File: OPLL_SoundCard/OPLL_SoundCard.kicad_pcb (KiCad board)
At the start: 2 copper layers, 101.6 x 53.3 mm, 13 parts, among them P1 Digital, P10 CONN_01X01, P11 CONN_01X01, P12 CONN_01X01, P13 CONN_01X01, P2 Power, P3 Analog, P4 Analog, P5 PWM, P6 PWM, P7 Communication, P8 CONN_01X01, P9 CONN_01X01

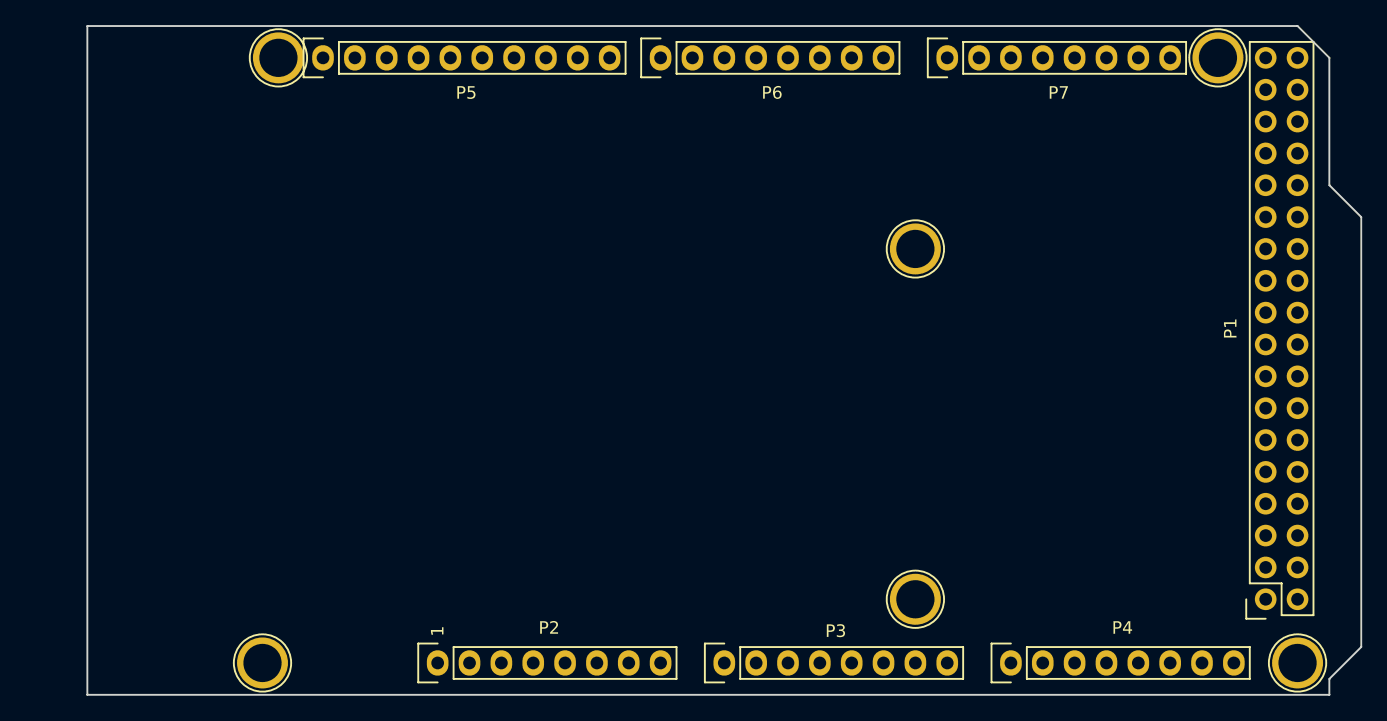
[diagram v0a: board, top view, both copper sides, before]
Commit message: PCB Soundcard
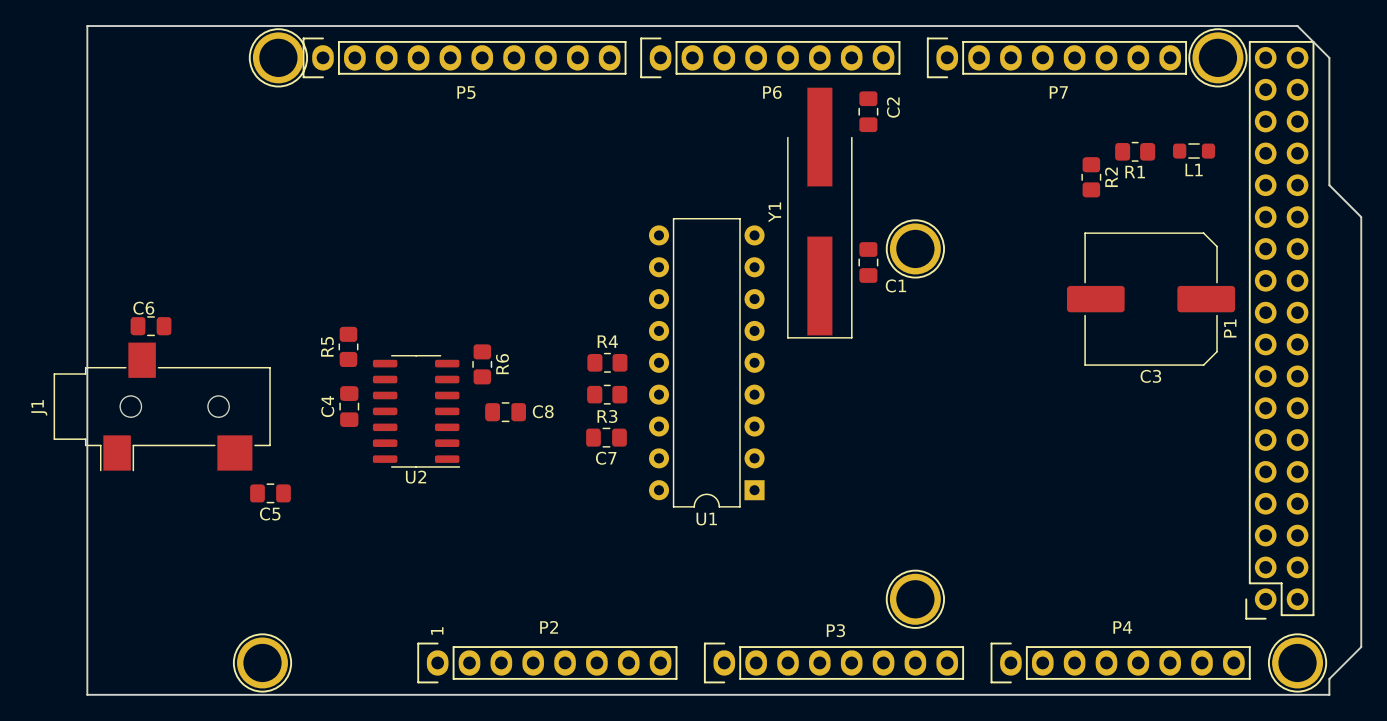
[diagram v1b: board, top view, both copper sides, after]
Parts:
- added C1: 15pF, Capacitor_SMD:C_0805_2012Metric_Pad1.18x1.45mm_HandSolder, F.Cu at (165.7, 87.2)
- added C2: 15pF, Capacitor_SMD:C_0805_2012Metric_Pad1.18x1.45mm_HandSolder, F.Cu at (165.7, 75.2)
- added C3: 1000uF, Capacitor_SMD:C_Elec_10x10.2, F.Cu at (188.2, 90.1)
- added C4: 15nF, Capacitor_SMD:C_0805_2012Metric_Pad1.18x1.45mm_HandSolder, F.Cu at (124.3, 98.7)
- added C5: 10uF, Capacitor_SMD:C_0805_2012Metric_Pad1.18x1.45mm_HandSolder, F.Cu at (118.0, 105.6)
- added C6: 10uF, Capacitor_SMD:C_0805_2012Metric_Pad1.18x1.45mm_HandSolder, F.Cu at (108.5, 92.3)
- added C7: .1uF, Capacitor_SMD:C_0805_2012Metric_Pad1.18x1.45mm_HandSolder, F.Cu at (144.8, 101.2)
- added C8: .1uF, Capacitor_SMD:C_0805_2012Metric_Pad1.18x1.45mm_HandSolder, F.Cu at (136.7, 99.1)
- added J1: AudioJack3, Connector_Audio:Jack_3.5mm_CUI_SJ-3523-SMT_Horizontal, F.Cu at (109.3, 98.7)
- added L1: 1mH, Inductor_SMD:L_0805_2012Metric_Pad1.05x1.20mm_HandSolder, F.Cu at (191.6, 78.3)
- added R1: 10k, Resistor_SMD:R_0805_2012Metric_Pad1.20x1.40mm_HandSolder, F.Cu at (186.9, 78.4)
- added R2: 4k7, Resistor_SMD:R_0805_2012Metric_Pad1.20x1.40mm_HandSolder, F.Cu at (183.5, 80.4)
- added R3: 2.2k, Resistor_SMD:R_0805_2012Metric_Pad1.20x1.40mm_HandSolder, F.Cu at (144.8, 97.7)
- added R4: 2.2k, Resistor_SMD:R_0805_2012Metric_Pad1.20x1.40mm_HandSolder, F.Cu at (144.9, 95.2)
- added R5: 4k7, Resistor_SMD:R_0805_2012Metric_Pad1.20x1.40mm_HandSolder, F.Cu at (124.2, 93.9)
- added R6: 2.2k, Resistor_SMD:R_0805_2012Metric_Pad1.20x1.40mm_HandSolder, F.Cu at (134.9, 95.3)
- added U1: YM2413B, Package_DIP:DIP-18_W7.62mm, F.Cu at (156.6, 105.3)
- added U2: LMC660, Package_SO:SOIC-14_3.9x8.7mm_P1.27mm, F.Cu at (129.6, 99.1)
- added Y1: 3.57MHz, Crystal:Crystal_SMD_HC49-SD_HandSoldering, F.Cu at (161.8, 83.1)
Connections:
- P1 pad 10: /47 -> (no net)
- P1 pad 11: /44 -> (no net)
- P1 pad 12: /45 -> (no net)
- P1 pad 13: /42 -> (no net)
- P1 pad 14: /43 -> (no net)
- P1 pad 15: /40 -> (no net)
- P1 pad 16: /41 -> (no net)
- P1 pad 17: /38 -> (no net)
- P1 pad 18: /39 -> (no net)
- P1 pad 19: /36 -> (no net)
- P1 pad 20: /37 -> (no net)
- P1 pad 21: /34 -> (no net)
- P1 pad 22: /35 -> (no net)
- P1 pad 23: /32 -> (no net)
- P1 pad 24: /33 -> (no net)
- P1 pad 25: /30 -> (no net)
- P1 pad 26: /31 -> (no net)
- P1 pad 27: /28 -> (no net)
- P1 pad 28: /29 -> (no net)
- P1 pad 29: /26 -> (no net)
- P1 pad 3: /52(SCK) -> (no net)
- P1 pad 30: /27 -> (no net)
- P1 pad 31: /24 -> (no net)
- P1 pad 32: /25 -> (no net)
- P1 pad 33: /22 -> (no net)
- P1 pad 34: /23 -> (no net)
- P1 pad 4: /53(SS) -> (no net)
- P1 pad 5: /50(MISO) -> (no net)
- P1 pad 6: /51(MOSI) -> (no net)
- P1 pad 7: /48 -> (no net)
- P1 pad 8: /49 -> (no net)
- P1 pad 9: /46 -> (no net)
- P10 pad 1: Net-(P10-Pad1) -> (no net)
- P11 pad 1: Net-(P11-Pad1) -> (no net)
- P12 pad 1: Net-(P12-Pad1) -> (no net)
- P13 pad 1: Net-(P13-Pad1) -> (no net)
- P2 pad 1: Net-(P2-Pad1) -> (no net)
- P2 pad 2: /IOREF -> (no net)
- P2 pad 3: /Reset -> (no net)
- P2 pad 4: +3V3 -> (no net)
- P2 pad 8: /Vin -> (no net)
- P3 pad 2: /A1 -> /~CS
- P3 pad 3: /A2 -> /~IC
- P3 pad 4: /A3 -> /~WE
- P3 pad 5: /A4 -> (no net)
- P3 pad 6: /A5 -> (no net)
- P3 pad 7: /A6 -> (no net)
- P3 pad 8: /A7 -> (no net)
- P4 pad 1: /A8 -> /D0
- P4 pad 2: /A9 -> /D1
- P4 pad 3: /A10 -> /D2
- P4 pad 4: /A11 -> /D3
- P4 pad 5: /A12 -> /D4
- P4 pad 6: /A13 -> /D5
- P4 pad 7: /A14 -> /D6
- P4 pad 8: /A15 -> /D7
- P5 pad 1: /SCL -> (no net)
- P5 pad 10: /8(**) -> (no net)
- P5 pad 2: /SDA -> (no net)
- P5 pad 3: /AREF -> (no net)
- P5 pad 5: /13(**) -> (no net)
- P5 pad 6: /12(**) -> (no net)
- P5 pad 7: /11(**) -> (no net)
- P5 pad 8: /10(**) -> (no net)
- P5 pad 9: /9(**) -> (no net)
- P6 pad 1: /7(**) -> (no net)
- P6 pad 2: /6(**) -> (no net)
- P6 pad 3: /5(**) -> (no net)
- P6 pad 4: /4(**) -> (no net)
- P6 pad 5: /3(**) -> (no net)
- P6 pad 6: /2(**) -> (no net)
- P6 pad 7: /1(Tx0) -> (no net)
- P6 pad 8: /0(Rx0) -> (no net)
- P7 pad 1: /14(Tx3) -> (no net)
- P7 pad 2: /15(Rx3) -> (no net)
- P7 pad 3: /16(Tx2) -> (no net)
- P7 pad 4: /17(Rx2) -> (no net)
- P7 pad 5: /18(Tx1) -> (no net)
- P7 pad 6: /19(Rx1) -> (no net)
- P7 pad 7: /20(SDA) -> (no net)
- P7 pad 8: /21(SCL) -> (no net)
- P8 pad 1: Net-(P8-Pad1) -> (no net)
- P9 pad 1: Net-(P9-Pad1) -> (no net)
